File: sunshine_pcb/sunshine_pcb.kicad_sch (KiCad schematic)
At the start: 46 parts, among them J2 Conn_01x04, J5 VerticalUSB, Q1 AO3400A, U1 ESP32-S3-WROOM-1, U2 SPX1117M3, U3 LIS3MDL, U4 ADXL375, U8 USBLC6-2P6

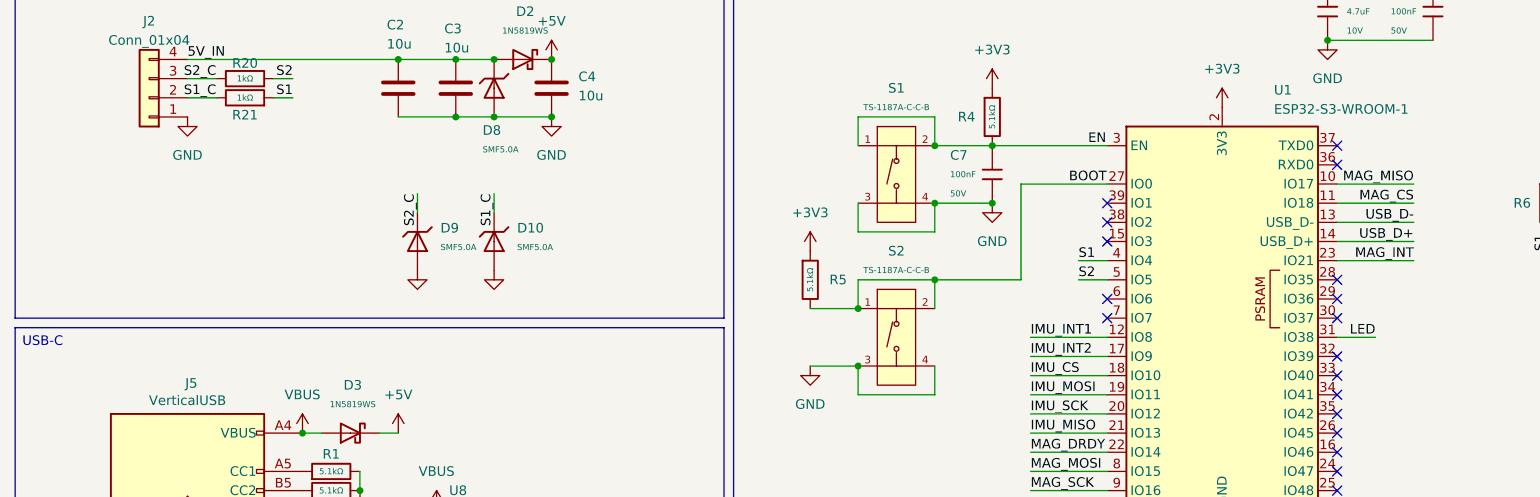
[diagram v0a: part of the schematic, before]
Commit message: Add voltage sense line
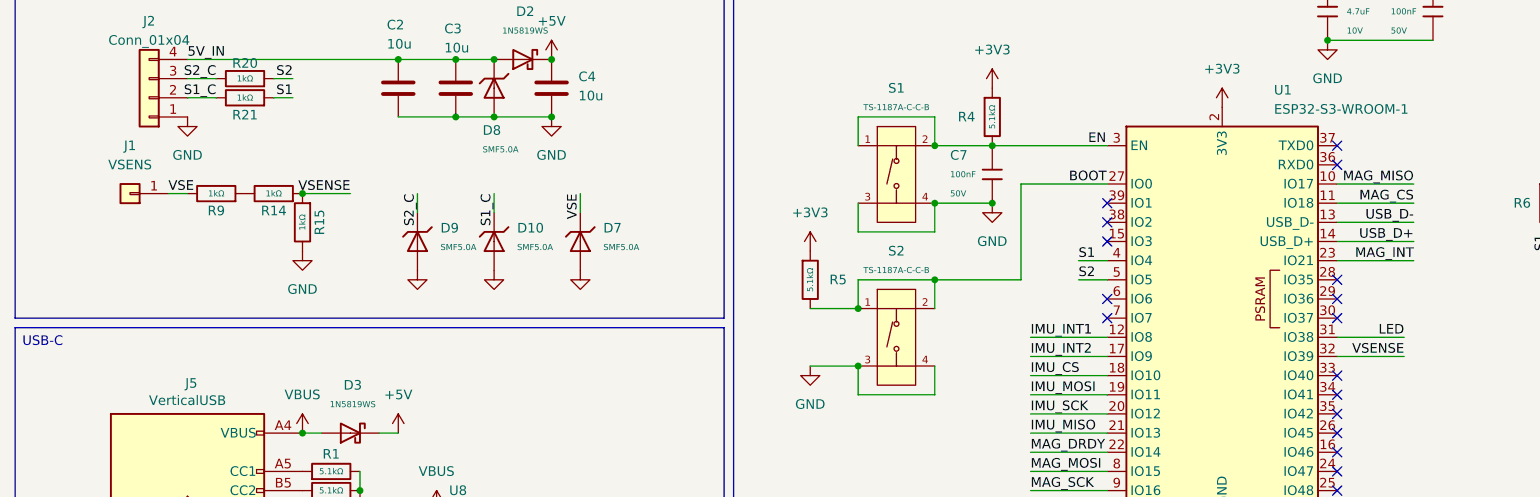
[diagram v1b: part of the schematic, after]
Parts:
- added D7: SMF5.0A, PCM_JLCPCB:D_SOD-123FL, symbol PCM_JLCPCB-Diodes:TVS-Uni,SMF5.0A
- added J1: VSENS, Connector_Wire:SolderWire-0.25sqmm_1x01_D0.65mm_OD1.7mm, symbol Connector_Generic:Conn_01x01
- added R14, R15, R9: 1kΩ, PCM_JLCPCB:R_0402, symbol PCM_JLCPCB-Resistors:0402,1kΩ
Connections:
- net GND: now also D7.2, R15.2
- net VSENSE: now reaches U1.32 (IO39)
- net VSENSE: now also R14.1, R15.1
- new net: R14.2, R9.1
- new net VSE: D7.1, J1.1 (Pin_1), R9.2
- no-connect marks 22 -> 21

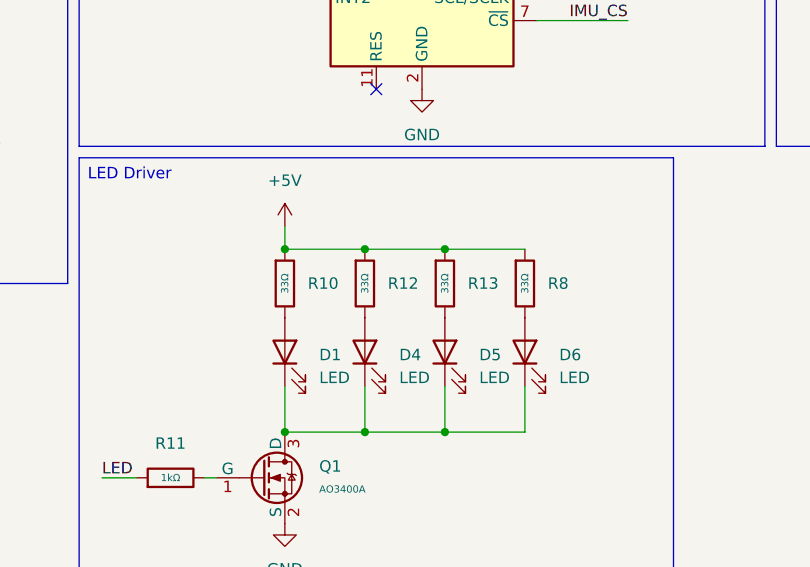
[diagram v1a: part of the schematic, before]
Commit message: Use brighter LED
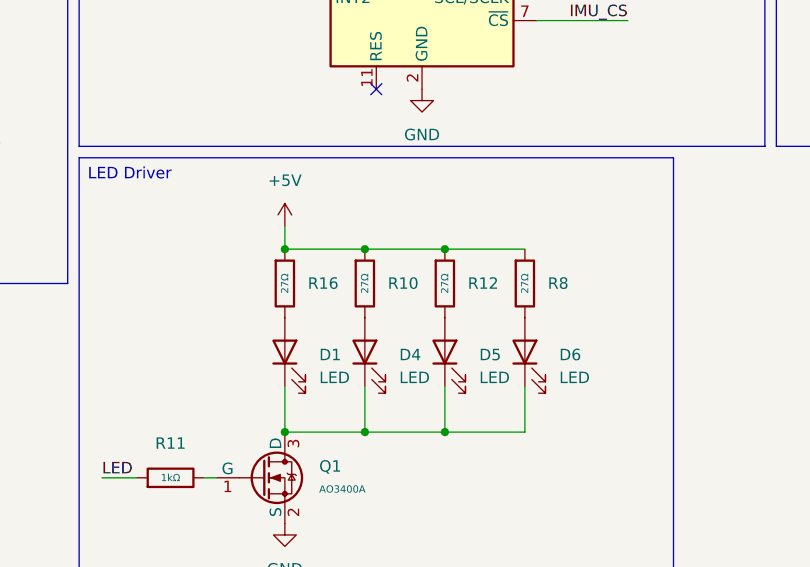
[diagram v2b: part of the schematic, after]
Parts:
- removed R10, R12, R13, R8: 33Ω, PCM_JLCPCB:R_0805, symbol PCM_JLCPCB-Resistors:0805,33Ω
- added R10, R12, R16, R8: 27Ω, PCM_JLCPCB:R_0805, symbol PCM_JLCPCB-Resistors:0805,27Ω
- D1, D4, D5, D6: LCSC C2843871 -> C2843876
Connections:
- net +5V: now also R10.1, R12.1, R16.1, R8.1
- net at D4.2 (A): now also R10.2
- net at D6.2 (A): now also R8.2
- net at D1.2 (A): now also R16.2
- net at D5.2 (A): now also R12.2

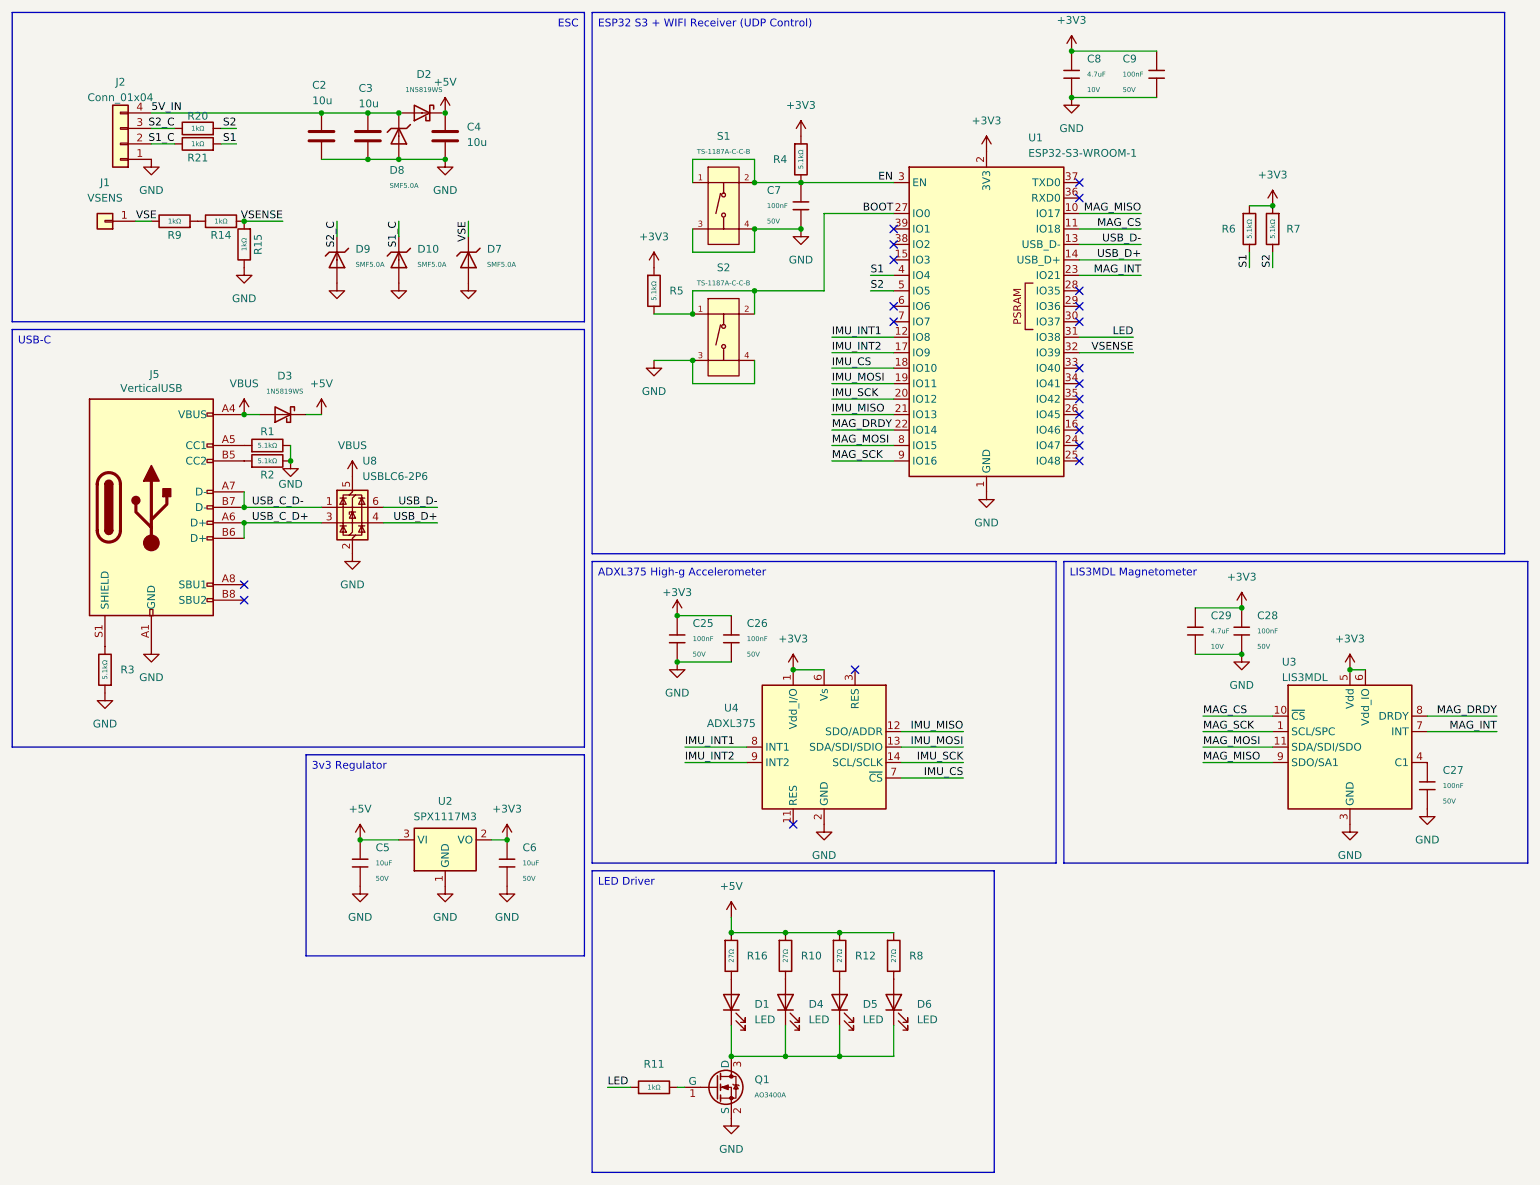
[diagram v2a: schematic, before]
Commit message: Update design for new switch
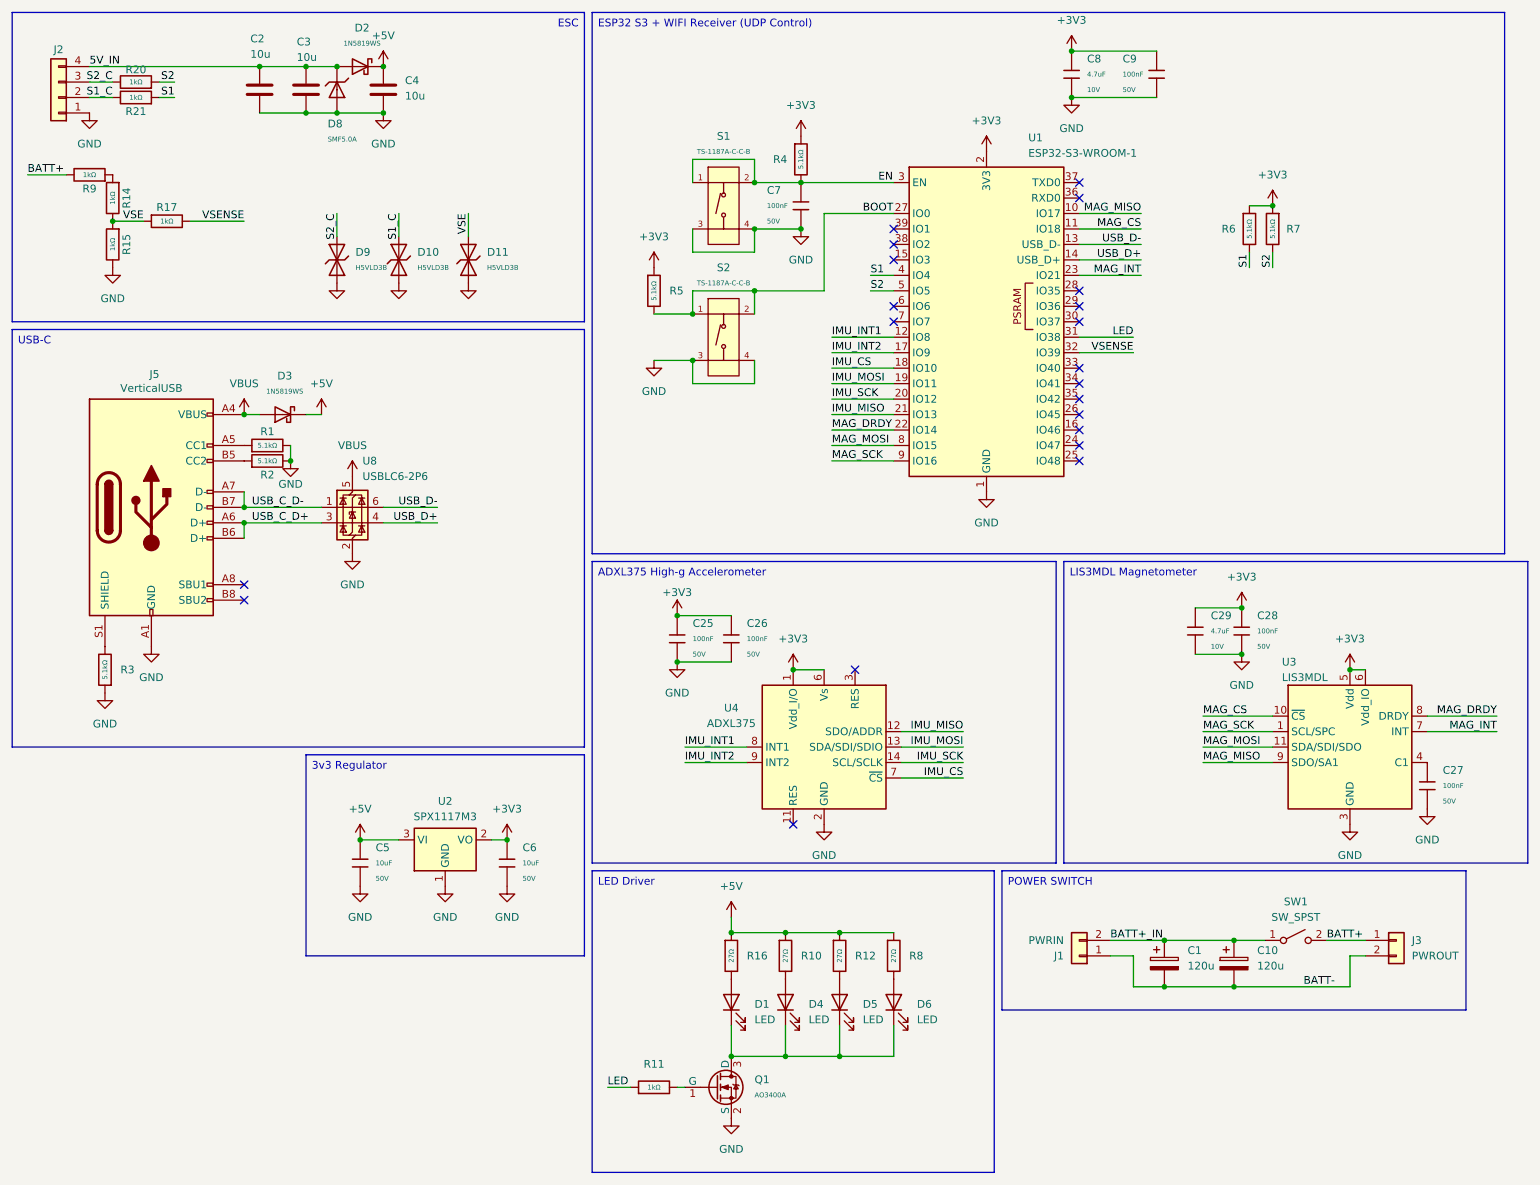
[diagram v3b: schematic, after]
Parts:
- removed D10, D7, D9: SMF5.0A, PCM_JLCPCB:D_SOD-123FL, symbol PCM_JLCPCB-Diodes:TVS-Uni,SMF5.0A
- removed J1: VSENS, Connector_Wire:SolderWire-0.25sqmm_1x01_D0.65mm_OD1.7mm, symbol Connector_Generic:Conn_01x01
- added C1, C10: 120u, Capacitor_THT:CP_Radial_D6.3mm_P2.50mm, symbol Device:C_Polarized
- added D10, D11, D9: H5VLD3B, PCM_JLCPCB:D_SOD-323, symbol PCM_JLCPCB-Diodes:TVS-Bi,H5VLD3B
- added J1: PWRIN, Connector_AMASS:AMASS_XT30PW-M_1x02_P2.50mm_Horizontal, symbol Connector_Generic:Conn_01x02
- added J3: PWROUT, SolderWire-1.5sqmm_1x02_P6mm_D1.7mm_OD3mm, symbol Connector_Generic:Conn_01x02
- added R17: 1kΩ, PCM_JLCPCB:R_0402, symbol PCM_JLCPCB-Resistors:0402,1kΩ
- added SW1: SW_SPST, custom:screw_switch, symbol Switch:SW_SPST
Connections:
- net GND: now also D10.1, D11.1, D9.1
- net S1_C: now also D10.2
- net S2_C: now also D9.2
- net VSE: now also R14.2, R15.1, D11.2, R17.1; no longer R9.2
- net VSENSE: now also R17.2; no longer R14.1, R15.1
- net at R9.1: now also R14.1; no longer R14.2
- new net BATT+: J3.1 (Pin_1), R9.2, SW1.2 (B)
- new net BATT+_IN: C1.1, C10.1, J1.2 (Pin_2), SW1.1 (A)
- new net BATT-: C1.2, C10.2, J1.1 (Pin_1), J3.2 (Pin_2)
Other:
- moved on the sheet: C2, C3, C4, D2, D8, J2, R14, R15, R20, R21, R9

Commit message: Re-layout PCB
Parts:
- removed C10: 120u, Capacitor_THT:CP_Radial_D6.3mm_P2.50mm, symbol Device:C_Polarized
- removed C2: 10u, Capacitor_SMD:C_1210_3225Metric, symbol Device:C
- removed R14, R9: 1kΩ, PCM_JLCPCB:R_0402, symbol PCM_JLCPCB-Resistors:0402,1kΩ
- added C2: 120u, Capacitor_THT:CP_Radial_D6.3mm_P2.50mm, symbol Device:C_Polarized
- added R13: 2kΩ, PCM_JLCPCB:R_0402, symbol PCM_JLCPCB-Resistors:0402,2kΩ
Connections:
- net BATT+: now also R13.1
- net BATT+_IN: now also C2.1
- net BATT-: now also C2.2
- net VSE: now also R13.2
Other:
- moved on the sheet: C1

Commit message: Update schematic
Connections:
- net VSENSE: now also U1.7 (IO7); no longer U1.32 (IO39)
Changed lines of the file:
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@@
-	)
-	(no_connect
-		(at 158.75 64.77)
 	)
 	(no_connect
@@
 	)
 	(no_connect
+		(at 189.23 69.85)
+	)
+	(no_connect
 		(at 189.23 44.45)
 	)
@@
 	(wire
 		(pts
-			(xy 189.23 69.85) (xy 198.12 69.85)
-		)
-		(stroke
-			(width 0)
-			(type default)
-		)
-	)
-	(wire
-		(pts
 			(xy 30.48 27.94) (xy 26.67 27.94)
 		)
@@
 		(pts
 			(xy 135.89 74.93) (xy 135.89 71.12)
+		)
+		(stroke
+			(width 0)
+			(type default)
+		)
+	)
+	(wire
+		(pts
+			(xy 148.59 64.77) (xy 158.75 64.77)
 		)
 		(stroke
@@
 		)
 	)
+	(label "VSENSE"
+		(at 148.59 64.77 0)
+		(effects
+			(font
+				(size 1.27 1.27)
+			)
+			(justify left bottom)
+		)
+	)
 	(label "BATT+"
 		(at 229.87 166.37 0)
@@
 		(effects
 			(font
-				(size 1.27 1.27)
-			)
-			(justify right bottom)
-		)
-	)
-	(label "VSENSE"
-		(at 198.12 69.85 180)
-		(effects
-			(font
